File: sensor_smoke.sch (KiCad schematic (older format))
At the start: 0 parts

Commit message: Added Smoke Sensor
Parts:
- added C501, C502, C508: 1u, Capacitor_SMD:C_0603_1608Metric, symbol Device:C_Small
- added C503: 10u, Capacitor_SMD:C_1206_3216Metric, symbol Device:C_Small
- added C504, C506, C507: 10u, Capacitor_SMD:C_0603_1608Metric, symbol Device:C_Small
- added C505: .1u, Capacitor_SMD:C_0402_1005Metric, symbol Device:C_Small
- added D501: D_Photo_ALT, symbol Device:D_Photo_ALT
- added FB501: 120, symbol Device:Ferrite_Bead_Small
- added R501: 1M, Resistor_SMD:R_0603_1608Metric, symbol Device:R_US
- added TP501, TP502: TestPoint, symbol Connector:TestPoint
- added U501: TLV70018_SOT23-5, Package_TO_SOT_SMD:SOT-23-5, symbol Regulator_Linear:TLV70018_SOT23-5
- added U502: ADPD188BI, symbol adpd188bi:ADPD188BI
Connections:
- net labels added: +1V8, +3.3V, +5V, GND, I2C_SCL, I2C_SDA
- wire segments 0 -> 63
- no-connect marks 0 -> 3

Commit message: Minor smoke cleanup
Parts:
- C504: value 10u -> 0.1u; Digikey 445-6853-1-ND -> 1292-1643-1-ND; MPN C1608X5R1A106M080AC -> 0603B104K500CT; Note CAP CER 10UF 10V X5R 0603 -> CAP CER 0.1UF 50V X7R 0603
- C505: value .1u -> 0.1u; footprint Capacitor_SMD:C_0402_1005Metric -> Capacitor_SMD:C_0603_1608Metric; Digikey 311-1336-1-ND -> 1292-1643-1-ND; Error 10% -> (none); LCSC C129131 -> (none); MPN CC0402KRX5R6BB104 -> 0603B104K500CT; Note CAP CER 0.1UF 10V X5R 0402 -> CAP CER 0.1UF 50V X7R 0603
- D501: value D_Photo_ALT -> Photodiode alt; footprint (none) -> LED_THT:LED_D3.0mm_Clear; Digikey (none) -> 1080-1140-ND; LCSC (none) -> C264281; MPN (none) -> PD204-6C; Note (none) -> SENSOR PHOTODIODE 940NM RADIAL
- U502: footprint (none) -> mylib:ADPD188BI; symbol adpd188bi:ADPD188BI -> mylib:ADPD188BI; Digikey (none) -> ADPD188BI-ACEZR7; MPN (none) -> ADPD188BI-ACEZR7; Note (none) -> SENSOR SMOKE 470NM/850NM AMB 24LGA
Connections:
- no-connect marks 3 -> 5
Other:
- moved on the sheet: C507, FB501

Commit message: Minor part picking and annotation
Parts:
- TP501, TP502: DNP (none) -> 1
- U501: value TLV70018_SOT23-5 -> TLV70018; footprint Package_TO_SOT_SMD:SOT-23-5 -> Package_TO_SOT_SMD:SOT-353_SC-70-5; Digikey (none) -> 296-32409-1-ND; LCSC (none) -> C133796; MPN (none) -> TLV70018DCK; Manufacturer (none) -> Texas Instruments; Note (none) -> IC REG LINEAR 1.8V 200MA SC70-5
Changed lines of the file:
@@
 P 2500 1700
 F 0 "U501" H 2500 2042 50  0000 C CNN
-F 1 "TLV70018_SOT23-5" H 2500 1951 50  0000 C CNN
-F 2 "Package_TO_SOT_SMD:SOT-23-5" H 2500 2025 50  0001 C CIN
+F 1 "TLV70018" H 2500 1951 50  0000 C CNN
+F 2 "Package_TO_SOT_SMD:SOT-353_SC-70-5" H 2500 2025 50  0001 C CIN
 F 3 "http://www.ti.com/lit/ds/symlink/tlv700.pdf" H 2500 1750 50  0001 C CNN
+F 4 "296-32409-1-ND" H 2500 1700 50  0001 C CNN "Digikey"
+F 5 "C133796" H 2500 1700 50  0001 C CNN "LCSC"
+F 6 "TLV70018DCK" H 2500 1700 50  0001 C CNN "MPN"
+F 7 "IC REG LINEAR 1.8V 200MA SC70-5" H 2500 1700 50  0001 C CNN "Note"
+F 8 "Texas Instruments" H 2500 1700 50  0001 C CNN "Manufacturer"
 	1    2500 1700
 	1    0    0    -1
@@
 F 2 "" H 7150 3700 50  0001 C CNN
 F 3 "~" H 7150 3700 50  0001 C CNN
+F 4 "1" H 6950 3700 50  0001 C CNN "DNP"
 	1    6950 3700
 	0    1    1    0
@@
 F 2 "" H 7150 3800 50  0001 C CNN
 F 3 "~" H 7150 3800 50  0001 C CNN
+F 4 "1" H 6950 3800 50  0001 C CNN "DNP"
 	1    6950 3800
 	0    1    1    0

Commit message: Major power changes
Added 5v boost, 3.3 buck, ideal diode circuits.
Poe: added barrel jacks
Smoke: general cleanup
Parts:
- removed C503: 10u, Capacitor_SMD:C_1206_3216Metric, symbol Device:C_Small
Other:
- moved on the sheet: R501, TP501, TP502
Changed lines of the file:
@@
 $Descr A4 11693 8268
 encoding utf-8
-Sheet 7 7
+Sheet 7 8
 Title ""
 Date ""
@@
 L power:+1V8 #PWR0502
 U 1 1 5FA659F5
-P 3400 1500
-F 0 "#PWR0502" H 3400 1350 50  0001 C CNN
-F 1 "+1V8" H 3415 1673 50  0000 C CNN
-F 2 "" H 3400 1500 50  0001 C CNN
-F 3 "" H 3400 1500 50  0001 C CNN
-	1    3400 1500
+P 3100 1500
+F 0 "#PWR0502" H 3100 1350 50  0001 C CNN
+F 1 "+1V8" H 3115 1673 50  0000 C CNN
+F 2 "" H 3100 1500 50  0001 C CNN
+F 3 "" H 3100 1500 50  0001 C CNN
+	1    3100 1500
 	1    0    0    -1
 $EndComp
@@
 	2900 1600 2800 1600
 Wire Wire Line
-	3400 1500 3400 1600
-Wire Wire Line
-	3400 1600 3200 1600
+	3100 1500 3100 1600
 Connection ~ 2900 1600
 NoConn ~ 4700 4150
@@
 Wire Wire Line
 	6350 4400 6350 4500
-$Comp
-L power:+1V8 #PWR0512
-U 1 1 5FA944B4
-P 6800 4050
-F 0 "#PWR0512" H 6800 3900 50  0001 C CNN
-F 1 "+1V8" H 6815 4223 50  0000 C CNN
-F 2 "" H 6800 4050 50  0001 C CNN
-F 3 "" H 6800 4050 50  0001 C CNN
-	1    6800 4050
-	1    0    0    -1
-$EndComp
-Wire Wire Line
-	6350 4200 6100 4200
+Wire Wire Line
+	6250 4200 6100 4200
 $Comp
 L Device:C_Small C?
@@
 	4500 3300 4500 3350
 Wire Wire Line
-	6650 4200 6800 4200
-Wire Wire Line
-	6800 4050 6800 4200
-Wire Wire Line
 	4450 3600 4700 3600
 $Comp
 L Connector:TestPoint TP501
 U 1 1 5FAF5131
-P 6950 3700
-F 0 "TP501" V 6950 3888 50  0000 L CNN
-F 1 "TestPoint" V 6846 3772 50  0001 C CNN
-F 2 "" H 7150 3700 50  0001 C CNN
-F 3 "~" H 7150 3700 50  0001 C CNN
-F 4 "1" H 6950 3700 50  0001 C CNN "DNP"
-	1    6950 3700
+P 6200 3700
+F 0 "TP501" V 6200 3888 50  0000 L CNN
+F 1 "TestPoint" V 6096 3772 50  0001 C CNN
+F 2 "" H 6400 3700 50  0001 C CNN
+F 3 "~" H 6400 3700 50  0001 C CNN
+F 4 "1" H 6200 3700 50  0001 C CNN "DNP"
+	1    6200 3700
 	0    1    1    0
 $EndComp
@@
 L Connector:TestPoint TP502
 U 1 1 5FAF78A5
-P 6950 3800
-F 0 "TP502" V 6950 3988 50  0000 L CNN
-F 1 "TestPoint" V 6995 3988 50  0001 L CNN
-F 2 "" H 7150 3800 50  0001 C CNN
-F 3 "~" H 7150 3800 50  0001 C CNN
-F 4 "1" H 6950 3800 50  0001 C CNN "DNP"
-	1    6950 3800
+P 6200 3800
+F 0 "TP502" V 6200 3988 50  0000 L CNN
+F 1 "TestPoint" V 6245 3988 50  0001 L CNN
+F 2 "" H 6400 3800 50  0001 C CNN
+F 3 "~" H 6400 3800 50  0001 C CNN
+F 4 "1" H 6200 3800 50  0001 C CNN "DNP"
+	1    6200 3800
 	0    1    1    0
-$EndComp
-$Comp
-L Device:C_Small C?
-U 1 1 5FB1E936
-P 3200 1850
-AR Path="/5E360A9B/5FB1E936" Ref="C?"  Part="1"
-AR Path="/5FB1E936" Ref="C?"  Part="1"
-AR Path="/5E5C8043/5E5C885F/5FB1E936" Ref="C?"  Part="1"
-AR Path="/5E5C8043/5E9EE9F0/5FB1E936" Ref="C?"  Part="1"
-AR Path="/5E5C8043/5EA19CBA/5FB1E936" Ref="C?"  Part="1"
-AR Path="/5E5C8043/5E49A000/5FB1E936" Ref="C?"  Part="1"
-AR Path="/5E5C8043/5EAB3002/5FB1E936" Ref="C?"  Part="1"
-AR Path="/5E5C8043/5FB1E936" Ref="C?"  Part="1"
-AR Path="/5F9DB5BA/5FB1E936" Ref="C503"  Part="1"
-F 0 "C503" H 3108 1896 50  0000 R CNN
-F 1 "10u" H 3108 1805 50  0000 R CNN
-F 2 "Capacitor_SMD:C_1206_3216Metric" H 3200 1850 50  0001 C CNN
-F 3 "~" H 3200 1850 50  0001 C CNN
-F 4 "CL31A106MAHNNNE" H 3200 1850 50  0001 C CNN "MPN"
-F 5 "1276-1181-1-ND" H 3200 1850 50  0001 C CNN "Digikey"
-F 6 "CAP CER 10UF 25V X5R 1206" H 3200 1850 50  0001 C CNN "Note"
-	1    3200 1850
-	-1   0    0    -1
-$EndComp
-Wire Wire Line
-	3200 1600 3200 1750
-Connection ~ 3200 1600
-Wire Wire Line
-	3200 1600 2900 1600
-Wire Wire Line
-	3200 1950 3200 2100
-$Comp
-L power:GND #PWR0506
-U 1 1 5FB21E3D
-P 3200 2100
-F 0 "#PWR0506" H 3200 1850 50  0001 C CNN
-F 1 "GND" H 3205 1927 50  0000 C CNN
-F 2 "" H 3200 2100 50  0001 C CNN
-F 3 "" H 3200 2100 50  0001 C CNN
-	1    3200 2100
-	1    0    0    -1
 $EndComp
 $Comp
@@
 L Device:R_US R?
 U 1 1 5FB53BAA
-P 6500 4200
+P 6400 4200
 AR Path="/5FB53BAA" Ref="R?"  Part="1"
 AR Path="/5F9DB5BA/5FB53BAA" Ref="R501"  Part="1"
-F 0 "R501" V 6705 4200 50  0000 C CNN
-F 1 "1M" V 6614 4200 50  0000 C CNN
-F 2 "Resistor_SMD:R_0603_1608Metric" H 6500 4200 60  0001 C CNN
-F 3 "" H 6500 4200 60  0001 C CNN
-F 4 "311-1.00MHRCT-ND" H 6500 4200 50  0001 C CNN "Digikey"
-F 5 "RC0603FR-071ML" H 6500 4200 50  0001 C CNN "MPN"
-F 6 "RES SMD 1M OHM 1% 1/10W 0603" H 6500 4200 50  0001 C CNN "Note"
-	1    6500 4200
+F 0 "R501" V 6605 4200 50  0000 C CNN
+F 1 "1M" V 6514 4200 50  0000 C CNN
+F 2 "Resistor_SMD:R_0603_1608Metric" H 6400 4200 60  0001 C CNN
+F 3 "" H 6400 4200 60  0001 C CNN
+F 4 "311-1.00MHRCT-ND" H 6400 4200 50  0001 C CNN "Digikey"
+F 5 "RC0603FR-071ML" H 6400 4200 50  0001 C CNN "MPN"
+F 6 "RES SMD 1M OHM 1% 1/10W 0603" H 6400 4200 50  0001 C CNN "Note"
+	1    6400 4200
 	0    -1   -1   0
 $EndComp
@@
 Connection ~ 6550 3300
 Wire Wire Line
-	6100 3700 6950 3700
-Wire Wire Line
-	6950 3800 6100 3800
+	6100 3700 6200 3700
+Wire Wire Line
+	6200 3800 6100 3800
 Wire Wire Line
 	4500 2500 4500 2650
@@
 	1    0    0    -1
 $EndComp
+Wire Wire Line
+	6550 4200 6650 4200
+Wire Wire Line
+	6650 4150 6650 4200
+$Comp
+L power:+1V8 #PWR0512
+U 1 1 5FA944B4
+P 6650 4150
+F 0 "#PWR0512" H 6650 4000 50  0001 C CNN
+F 1 "+1V8" H 6665 4323 50  0000 C CNN
+F 2 "" H 6650 4150 50  0001 C CNN
+F 3 "" H 6650 4150 50  0001 C CNN
+	1    6650 4150
+	1    0    0    -1
+$EndComp
+Wire Wire Line
+	2900 1600 3100 1600
 $EndSCHEMATC

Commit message: Continue part picking
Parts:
- FB501: value 120 -> Ferrite_Bead_Small; footprint (none) -> Inductor_SMD:L_0603_1608Metric; Digikey (none) -> 490-5223-1-ND; LCSC (none) -> C97853; MPN (none) -> BLM18PG471SN1D; Mouser (none) -> 81-BLM18PG471SN1D; Note (none) -> 470 Ohms @ 100MHz 1 Power Line Ferrite Bead 0603 1A 200mOhm
- TP501, TP502: footprint (none) -> TestPoint:TestPoint_Pad_D1.0mm
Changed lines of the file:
@@
 U 1 1 5FA39D74
 P 4500 2750
-F 0 "FB501" H 4600 2796 50  0000 L CNN
-F 1 "120" H 4600 2705 50  0000 L CNN
-F 2 "" V 4430 2750 50  0001 C CNN
+F 0 "FB501" H 4600 2750 50  0000 L CNN
+F 1 "Ferrite_Bead_Small" H 4600 2705 50  0001 L CNN
+F 2 "Inductor_SMD:L_0603_1608Metric" V 4430 2750 50  0001 C CNN
 F 3 "~" H 4500 2750 50  0001 C CNN
+F 4 "490-5223-1-ND" H 4500 2750 50  0001 C CNN "Digikey"
+F 5 "C97853" H 4500 2750 50  0001 C CNN "LCSC"
+F 6 "BLM18PG471SN1D" H 4500 2750 50  0001 C CNN "MPN"
+F 7 "81-BLM18PG471SN1D " H 4500 2750 50  0001 C CNN "Mouser"
+F 8 "470 Ohms @ 100MHz 1 Power Line Ferrite Bead 0603 1A 200mOhm" H 4500 2750 50  0001 C CNN "Note"
 	1    4500 2750
 	1    0    0    -1
@@
 F 0 "TP501" V 6200 3888 50  0000 L CNN
 F 1 "TestPoint" V 6096 3772 50  0001 C CNN
-F 2 "" H 6400 3700 50  0001 C CNN
+F 2 "TestPoint:TestPoint_Pad_D1.0mm" H 6400 3700 50  0001 C CNN
 F 3 "~" H 6400 3700 50  0001 C CNN
 F 4 "1" H 6200 3700 50  0001 C CNN "DNP"
@@
 F 0 "TP502" V 6200 3988 50  0000 L CNN
 F 1 "TestPoint" V 6245 3988 50  0001 L CNN
-F 2 "" H 6400 3800 50  0001 C CNN
+F 2 "TestPoint:TestPoint_Pad_D1.0mm" H 6400 3800 50  0001 C CNN
 F 3 "~" H 6400 3800 50  0001 C CNN
 F 4 "1" H 6200 3800 50  0001 C CNN "DNP"

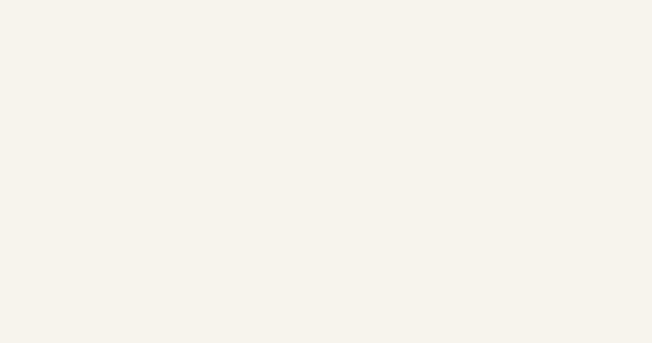
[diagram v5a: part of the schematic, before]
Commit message: Add smoke chamber to sch and layout
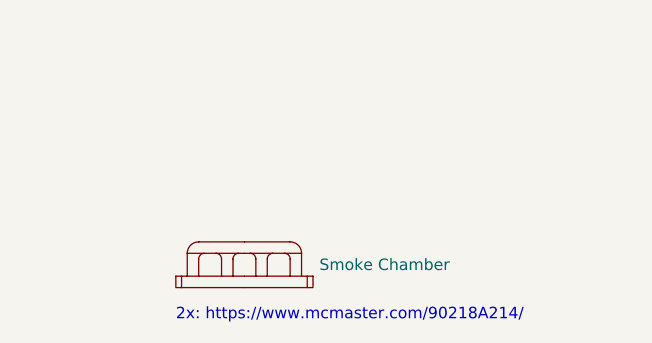
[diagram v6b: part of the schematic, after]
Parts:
- added U503: Smoke Chamber, mylib:ADPD188BI_Chamber, symbol mylib:Chamber
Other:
- note added: "2x: https://www.mcmaster.com/90218A214/"
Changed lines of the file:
@@
 Wire Wire Line
 	2900 1600 3100 1600
+$Comp
+L mylib:Chamber U503
+U 1 1 5FB92C1C
+P 7800 6150
+F 0 "U503" H 7800 6465 50  0001 C CNN
+F 1 "Smoke Chamber" H 8128 6200 50  0000 L CNN
+F 2 "mylib:ADPD188BI_Chamber" H 7800 6150 50  0001 C CNN
+F 3 "" H 7800 6150 50  0001 C CNN
+F 4 "3D printed smoke chamber" H 7800 6150 50  0001 C CNN "Note"
+F 5 "1" H 7800 6150 50  0001 C CNN "DNP"
+	1    7800 6150
+	1    0    0    -1
+$EndComp
+Text Notes 7500 6350 0    50   ~ 0
+2x: https://www.mcmaster.com/90218A214/
 $EndSCHEMATC
